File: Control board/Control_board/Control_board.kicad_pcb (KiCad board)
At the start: 2 copper layers, 55 parts, among them J1 KEYPAD, J2 UART_conn, J3 Power_IN, J4 SPI_conn, SW1 RESET, U1 AT45DB321E-SHF-T, U10 SP3485EN, U2 LM2576HVS-5, U4 Wifi, U5 LM1117LD-3.3, U6 STM32F103C8Tx, U7 RTC_DS3234, U8 DS3232SN-T&R, U9 OLED, Y1 8MHZ

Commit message: edit layout
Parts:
- added D7: DF02S, Diode_SMD:Diode_Bridge_OnSemi_SDIP-4L, F.Cu at (67.2, 58.9)
- added U3: LoRa, smart_meter:LoRa, F.Cu at (188.1, 119.8)
- TH1, TH2: value Thermistor_PTC -> 250-120U
- moved U4 165.1 mm to (145.7, 118.3)
- moved D1 144.1 mm to (103.2, 40.1)
- moved C10 131.4 mm to (111.0, 63.9)
- moved D5 130.0 mm to (113.8, 56.6)
- moved D6 129.7 mm to (113.8, 74.0)
- moved TH1 125.6 mm to (102.0, 73.2)
- moved R21 123.0 mm to (96.5, 63.9), turned to -90 degrees
- moved TH2 122.1 mm to (102.0, 55.8)
- moved U10 121.0 mm to (104.6, 64.9)
- moved R20 119.4 mm to (116.3, 63.9), turned to 90 degrees
- moved R22 119.4 mm to (116.3, 69.1), turned to 90 degrees
- moved J1 108.6 mm to (230.6, 30.5)
- moved SW1 108.3 mm to (156.0, 51.4)
- moved R19 108.3 mm to (157.0, 58.9)
- moved R5 76.8 mm to (127.0, 128.6), turned to -90 degrees
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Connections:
- J3 pad 1: /12V -> Net-(J3-Pin_1)
- J3 pad 2: /GND -> Net-(J3-Pin_2)

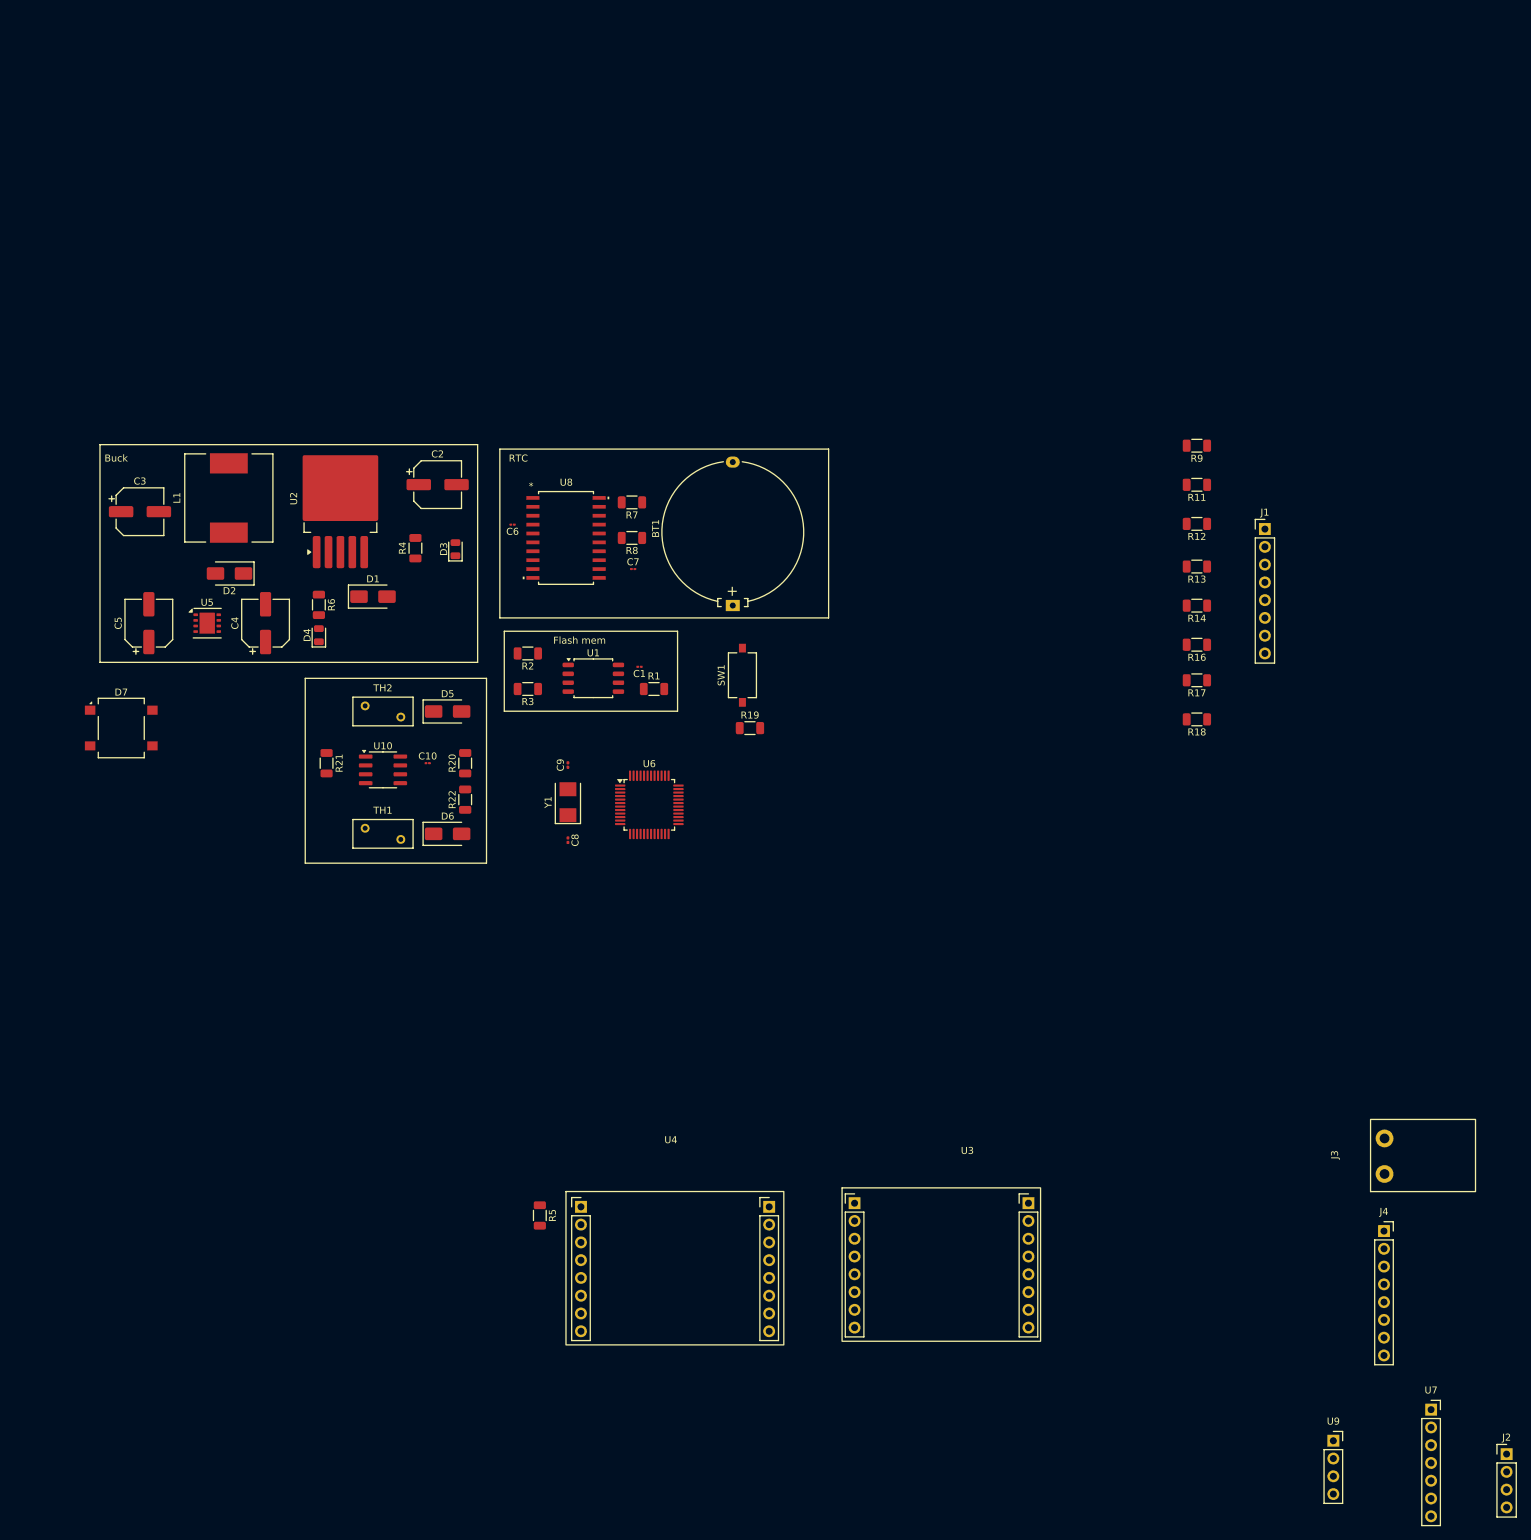
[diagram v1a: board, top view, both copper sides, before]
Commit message: Add ic to external GPIO
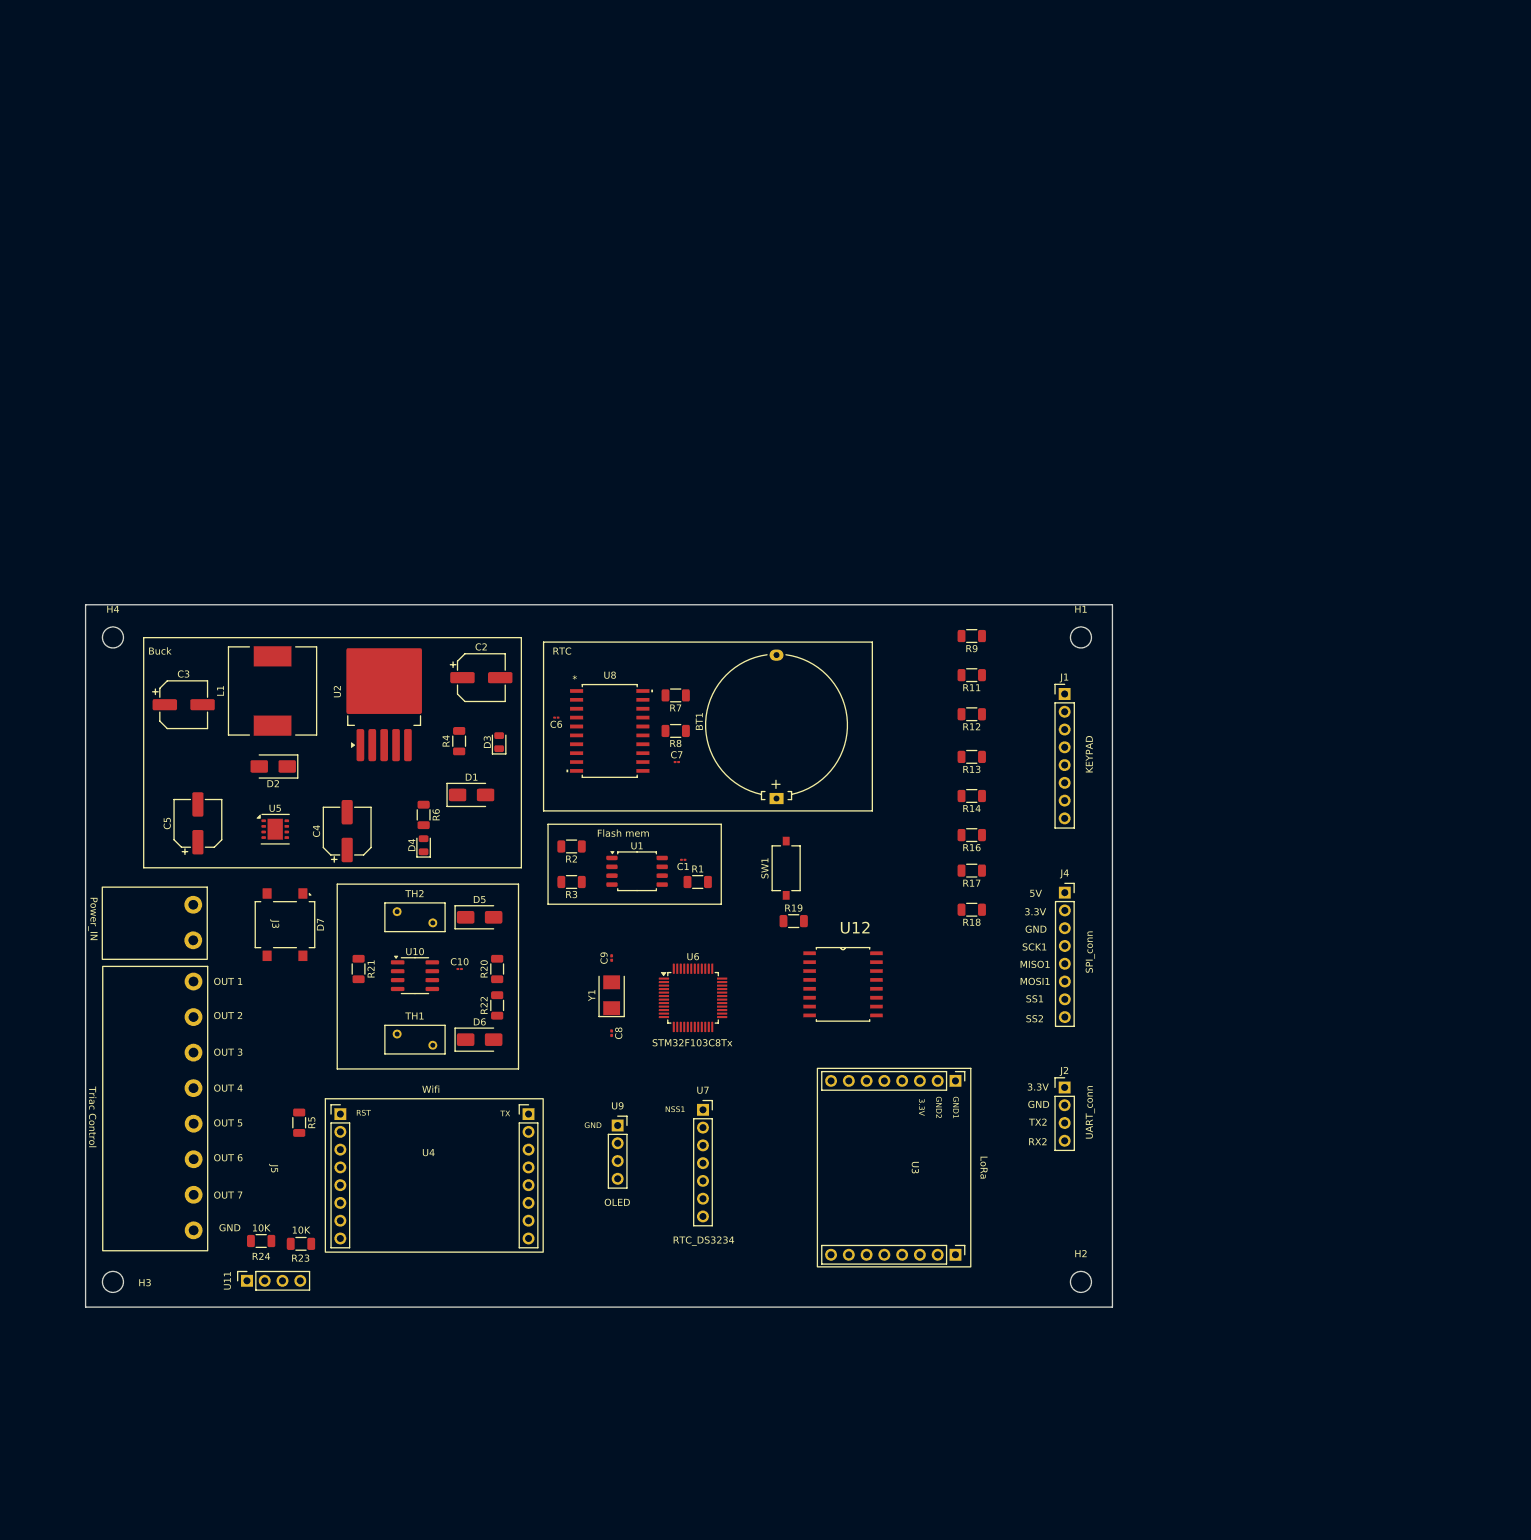
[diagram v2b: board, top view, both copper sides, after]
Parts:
- added H1: MountingHole, MountingHole:MountingHole_3mm, F.Cu at (204.3, 46.0)
- added H2: MountingHole, MountingHole:MountingHole_3mm, F.Cu at (204.3, 138.1)
- added H3: MountingHole, MountingHole:MountingHole_3mm, F.Cu at (66.0, 138.1)
- added H4: MountingHole, MountingHole:MountingHole_3mm, F.Cu at (66.0, 46.0)
- added J5: Triac Control, smart_meter:RC8, F.Cu at (85.7, 116.2)
- added R23: 10K, Resistor_SMD:R_1206_3216Metric, F.Cu at (92.9, 132.6)
- added R24: 10K, Resistor_SMD:R_1206_3216Metric, F.Cu at (87.2, 132.2)
- added U11: Debug, Connector_PinSocket_2.54mm:PinSocket_1x04_P2.54mm_Vertical, F.Cu at (85.1, 137.9)
- added U12: PCA9554AD_118, smart_meter:SOIC127P1032X265-16N, F.Cu at (170.3, 95.6)
- moved J3 160.5 mm to (84.1, 86.9), turned to -90 degrees
- moved U7 112.5 mm to (150.3, 113.5)
- moved U9 111.8 mm to (138.1, 115.7)
- moved J2 82.1 mm to (202.0, 110.3)
- moved J4 66.5 mm to (202.0, 82.4)
- moved R11 42.1 mm to (188.7, 51.4)
- moved R12 42.1 mm to (188.7, 56.9)
- moved R13 42.1 mm to (188.7, 63.0)
- moved R14 42.1 mm to (188.7, 68.6)
- moved R16 42.1 mm to (188.7, 74.2)
- moved R17 42.1 mm to (188.7, 79.3)
- moved R18 42.1 mm to (188.7, 84.9)
- moved R9 42.1 mm to (188.7, 45.8)
- moved J1 37.1 mm to (202.0, 54.1)
- moved U4 36.9 mm to (111.3, 105.0)
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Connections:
- D7 pad 3: Net-(J3-Pin_2) -> Net-(J3-Pin_1)
- D7 pad 4: Net-(J3-Pin_1) -> Net-(J3-Pin_2)
- U6 pad 18: /KEY1 -> /OUT1
- U6 pad 19: /KEY2 -> /OUT2
- U6 pad 20: /KEY3 -> /OUT3
- U6 pad 33: /GPIO_1 -> /RST_LoRa
- U6 pad 34: /GPIO_2 -> /SWDIO
- U6 pad 37: /RST_LoRa -> /SWCLK
- U6 pad 39: /KEY4 -> /OUT4
- U6 pad 4: unconnected-(U6-PC15-Pad4) -> /OUT7
- U6 pad 40: /KEY5 -> /OUT5
- U6 pad 41: /KEY6 -> /OUT6
- U6 pad 45: /KEY7 -> /GPIO_1
- U6 pad 46: /KEY8 -> /GPIO_2
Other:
- board outline added: 146.8 x 100.4 mm
- board text added: "3.3V"
- board text added: "5V"
- board text added: "GND"
- board text added: "GND1"
- board text added: "GND2"
- board text added: "MISO1"
- board text added: "MOSI1"
- board text added: "NSS1"
- board text added: "OUT 1"
- board text added: "OUT 2"
- board text added: "OUT 3"
- board text added: "OUT 4"
- board text added: "OUT 5"
- board text added: "OUT 6"
- board text added: "OUT 7"
- board text added: "RST"
- board text added: "RX2"
- board text added: "SCK1"
- board text added: "SS1"
- board text added: "SS2"
- board text added: "TX"
- board text added: "TX2"

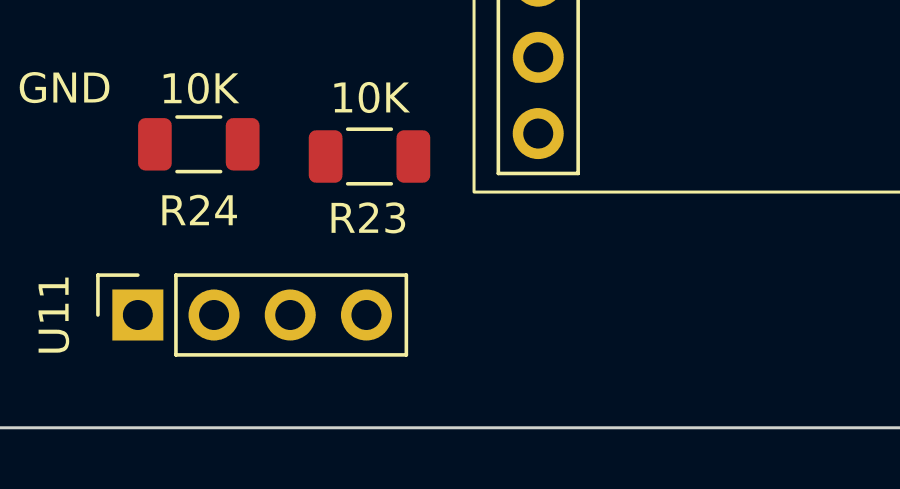
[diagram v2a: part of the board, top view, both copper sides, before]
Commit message: Routing Power ctr
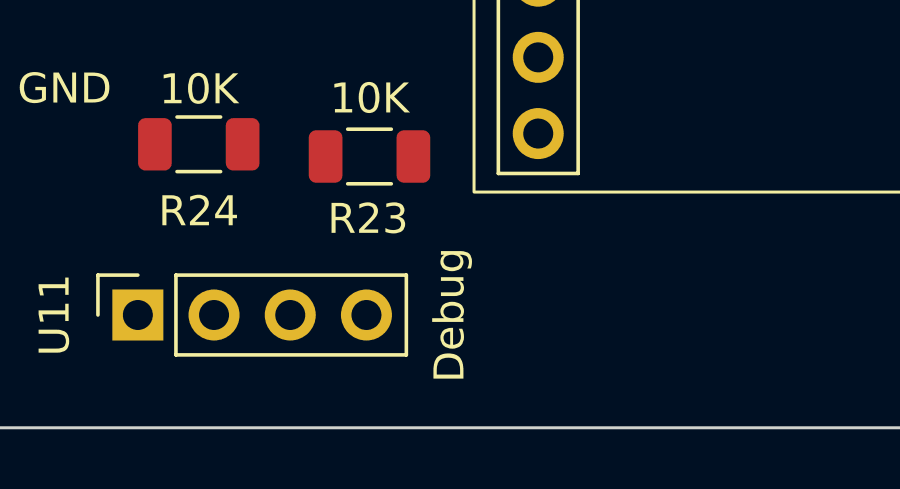
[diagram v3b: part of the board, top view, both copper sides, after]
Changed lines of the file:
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@@
 		(property "Value" "Debug"
 			(at 0 10.39 90)
-			(layer "F.Fab")
+			(layer "F.SilkS")
 			(effects
 				(font

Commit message: Routing control board
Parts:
- removed U5: LM1117LD-3.3, Package_SON:WSON-8-1EP_4x4mm_P0.8mm_EP2.2x3mm
- added D8: LED, LED_SMD:LED_0805_2012Metric, F.Cu at (99.4, 132.9)
- added D9: LED, LED_SMD:LED_0805_2012Metric, F.Cu at (99.4, 138.2)
- added J6: MDB, smart_meter:MDB, F.Cu at (79.3, 147.9)
- added JP1: TX1_selector, Connector_PinHeader_2.54mm:PinHeader_1x03_P2.54mm_Vertical, F.Cu at (96.1, 112.9)
- added JP2: RX1_Selector, Connector_PinHeader_2.54mm:PinHeader_1x03_P2.54mm_Vertical, F.Cu at (108.2, 113.0)
- added R10: 10K, Resistor_SMD:R_1206_3216Metric, F.Cu at (108.4, 127.2)
- added R15: 470, Resistor_SMD:R_1206_3216Metric, F.Cu at (108.3, 132.9)
- added R25: 10K, Resistor_SMD:R_1206_3216Metric, F.Cu at (181.5, 139.1)
- added R26: 10K, Resistor_SMD:R_1206_3216Metric, F.Cu at (165.7, 139.1)
- added R27: 390, Resistor_SMD:R_1206_3216Metric, F.Cu at (108.1, 138.2)
- added R28: 39, Resistor_SMD:R_1206_3216Metric, F.Cu at (99.3, 127.2)
- added R29: 680, Resistor_SMD:R_1206_3216Metric, F.Cu at (117.4, 127.5)
- added R30: 470, Resistor_SMD:R_1206_3216Metric, F.Cu at (117.4, 133.2)
- added R31: 2K, Resistor_SMD:R_1206_3216Metric, F.Cu at (117.4, 138.5)
- added SW2: Button1, Button_Switch_SMD:SW_Tactile_SPST_NO_Straight_CK_PTS636Sx25SMTRLFS, F.Cu at (181.8, 145.7)
- added SW3: Button2, Button_Switch_SMD:SW_Tactile_SPST_NO_Straight_CK_PTS636Sx25SMTRLFS, F.Cu at (166.4, 145.7)
- added T1: BCX17, smart_meter:BCX17, F.Cu at (92.0, 145.4)
- added T2: BCX17, smart_meter:BCX17, F.Cu at (91.9, 133.3)
- added U13: LM317DCY, smart_meter:LM3.3V, F.Cu at (89.8, 72.6)
- J2: footprint Connector_PinHeader_2.54mm:PinHeader_1x04_P2.54mm_Vertical -> smart_meter:RC4
- J4: footprint Connector_PinSocket_2.54mm:PinSocket_1x08_P2.54mm_Vertical -> smart_meter:RC8
- U12: footprint smart_meter:SOIC127P1032X265-16N -> smart_meter:PCA955
- moved U11 119.7 mm to (204.5, 147.6), turned to 180 degrees
- moved R24 106.7 mm to (192.7, 147.6), turned to -90 degrees
- moved R23 100.0 mm to (192.6, 140.7), turned to -90 degrees
- moved U7 39.8 mm to (124.5, 143.8), turned to 90 degrees
- moved U9 29.7 mm to (147.5, 143.9), turned to 90 degrees
- moved R5 26.3 mm to (118.9, 115.6)
- moved U4 26.3 mm to (137.6, 105.3)
- moved U3 25.5 mm to (175.3, 107.5), turned to 0 degrees
- moved J2 22.3 mm to (185.2, 124.9), turned to 90 degrees
- moved H2 18.1 mm to (204.0, 156.2)
- moved H3 18.1 mm to (66.3, 156.2)
- moved J4 17.7 mm to (185.4, 88.7), turned to 90 degrees
- moved J1 8.32 mm to (196.0, 48.3)
- moved R11 7.43 mm to (181.3, 51.3)
- moved R12 7.43 mm to (181.3, 56.8)
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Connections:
- U10 pad 1: /RX1 -> /RX_485
- U10 pad 4: /TX1 -> /TX_485
- U6 pad 2: unconnected-(U6-PC13-Pad2) -> /Button1
- U6 pad 3: unconnected-(U6-PC14-Pad3) -> /Button2
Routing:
- net /3.3V: track 0.00 -> 588.2 mm, vias 0 -> 6
- net /5V: track 0.00 -> 299.3 mm, vias 0 -> 2
- net /SCK1: track 0.00 -> 173.7 mm, vias 0 -> 4
- net /GND: track 0.00 -> 172.9 mm, vias 0 -> 39
- net /MISO1: track 0.00 -> 166.4 mm, vias 0 -> 4
- net /MOSI1: track 0.00 -> 150.9 mm, vias 0 -> 2
- net /SDA_1: track 0.00 -> 129.7 mm, vias 0 -> 2
- net /SCL_1: track 0.00 -> 125.5 mm, vias 0 -> 2
- net /SWCLK: track 0.00 -> 120.3 mm, vias 0 -> 2
- net /Button1: track 0.00 -> 118.1 mm, vias 0 -> 2
- net /SWDIO: track 0.00 -> 113.1 mm, vias 0 -> 4
- net /12V: track 0.00 -> 107.6 mm, vias 0 -> 1
- net /OUT4: track 0.00 -> 102.5 mm, vias 0 -> 2
- net /OUT7: track 0.00 -> 97.3 mm, vias 0 -> 2
- net /OUT6: track 0.00 -> 92.3 mm, vias 0 -> 2
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- added copper zone on B.Cu, net /GND
- added copper zone on F.Cu, net /GND
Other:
- board size 146.8 x 100.4 mm -> 146.8 x 119 mm
- board text added: "3.3"
- board text added: "MDB"
- board text added: "RS485"
- board text added: "SWCLK"
- board text added: "SWDIO"
